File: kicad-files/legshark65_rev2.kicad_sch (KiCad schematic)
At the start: 199 parts, among them J1 ARM JTAG, SW1 K2-1187SQ-A4SW-06, SW2 PCM12SMTR, T2 53261-0471, U1 STM32F411CEU6, U2 MCP1700T-3302E/TT, U3 AT24C256C-SSHL-T, Y1 TAXM8M4RFDCET2T

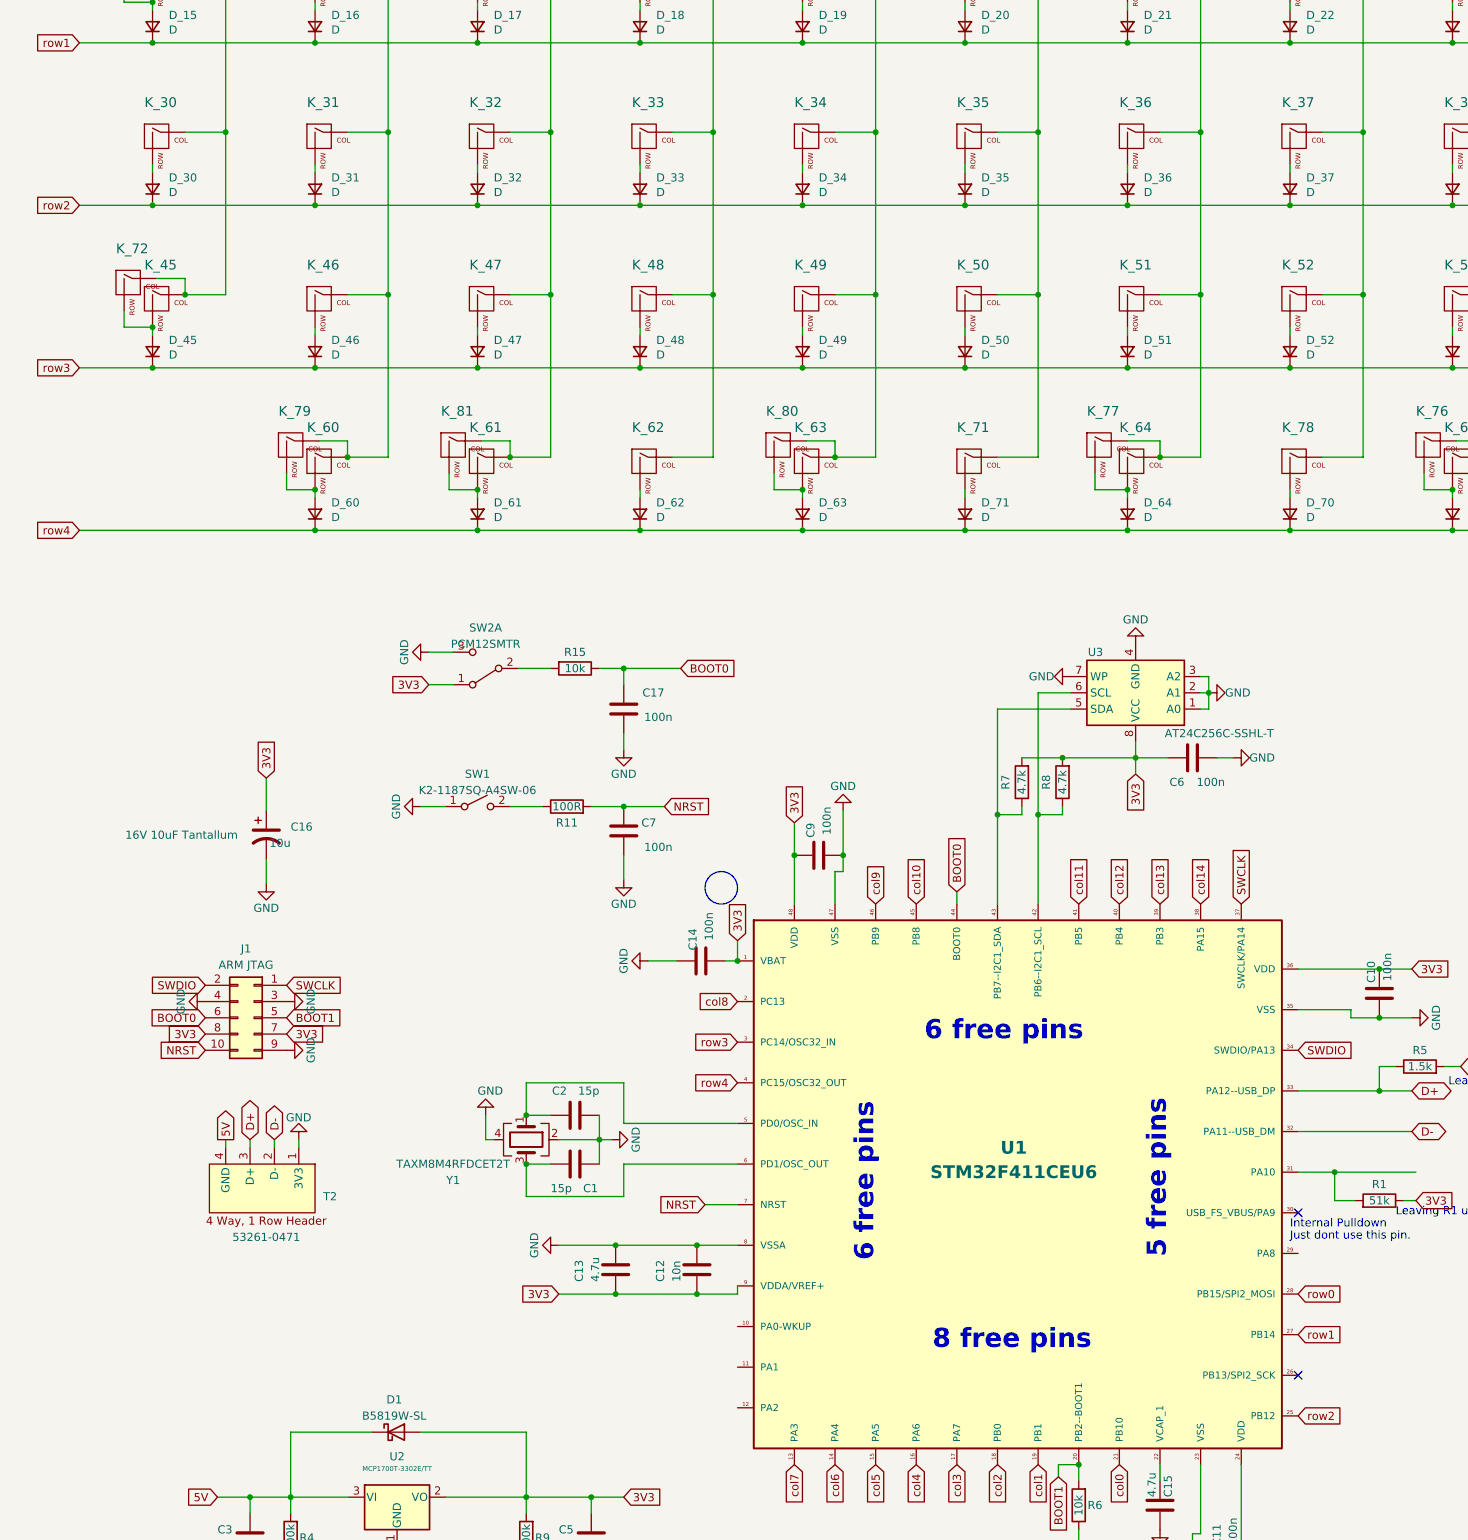
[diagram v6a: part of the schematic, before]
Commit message: Making the tracks have a more consistant width
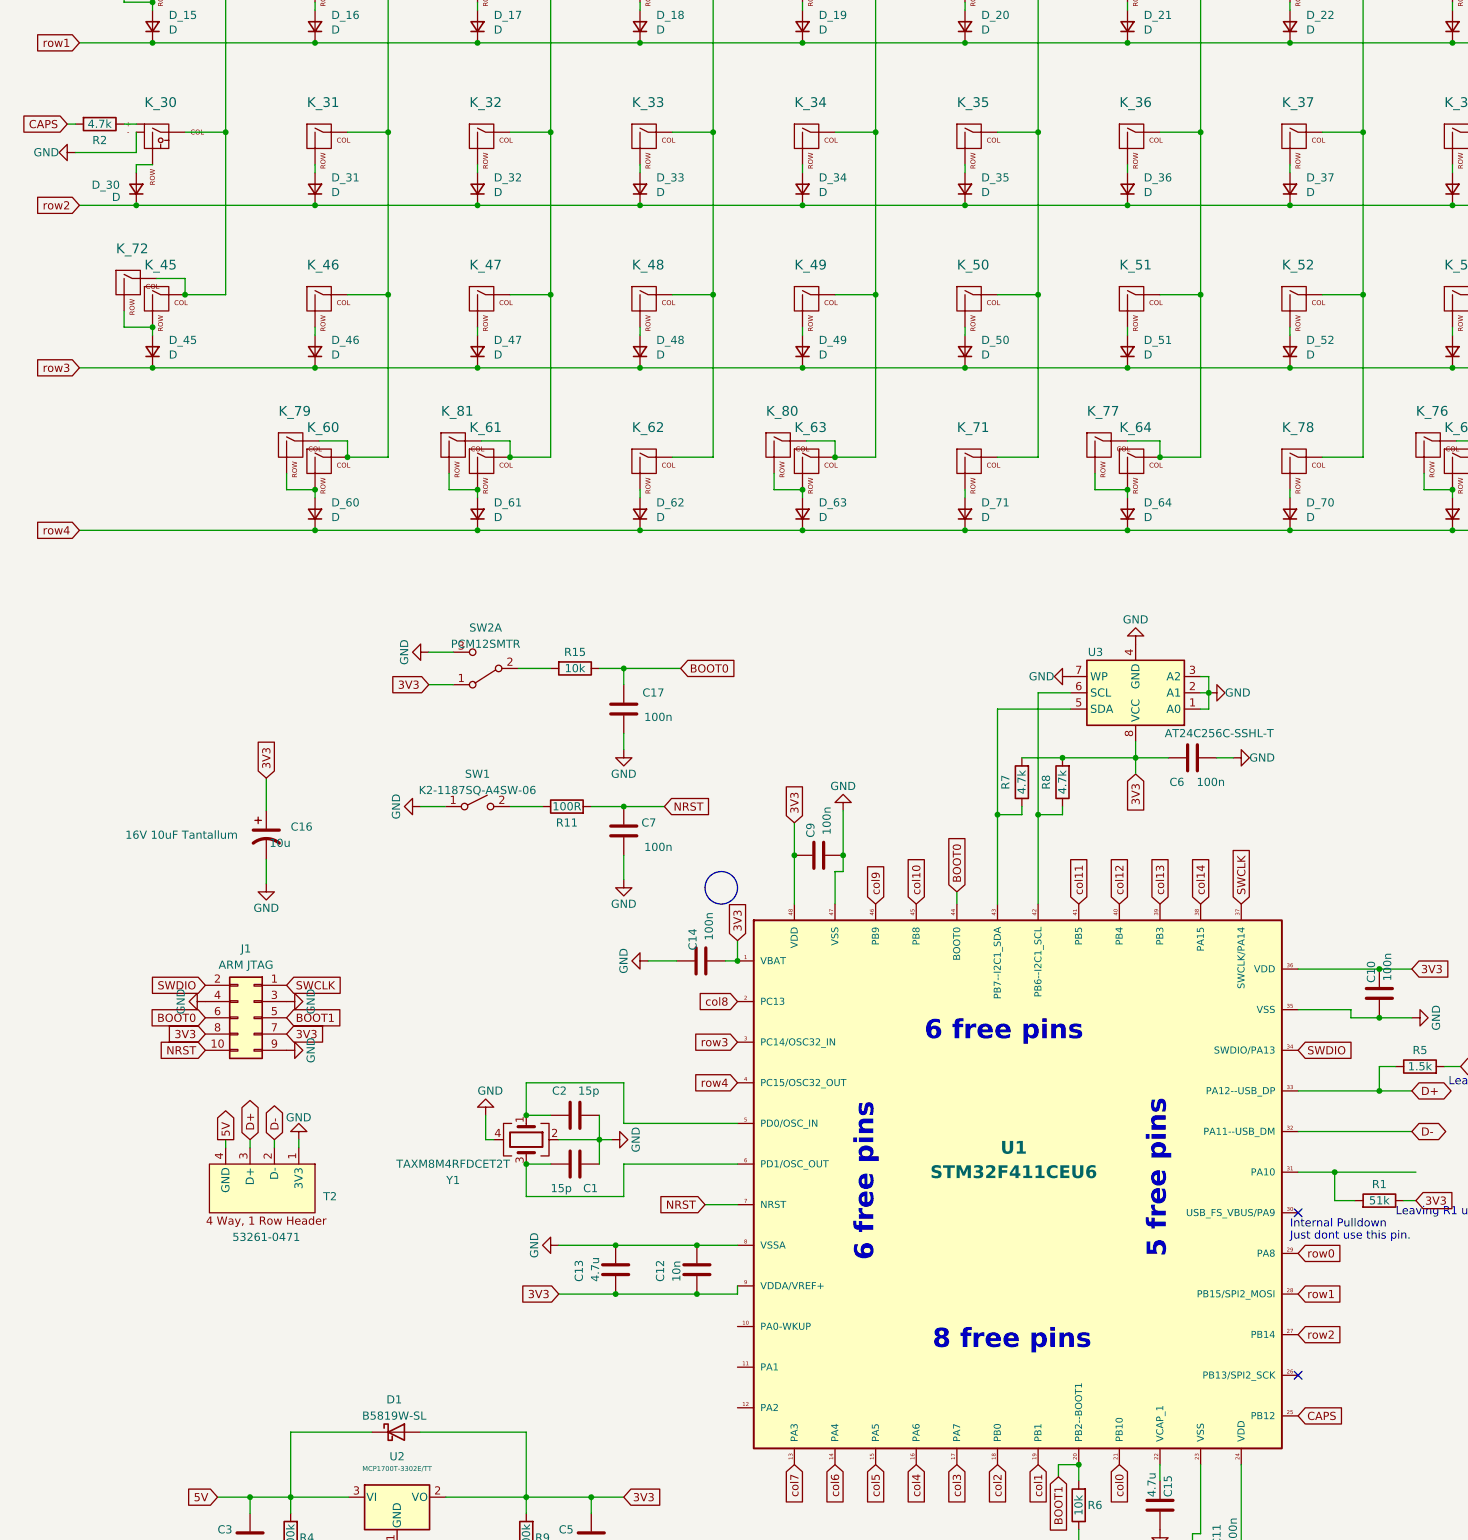
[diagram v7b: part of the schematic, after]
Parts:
- added R2: 4.7k, Resistor_SMD:R_0402_1005Metric_Pad0.72x0.64mm_HandSolder, symbol Device:R
- K_30: footprint MX_Only:MXOnly-1U-NoLED -> MX_Only:MXOnly-1U; symbol MX_Alps_Hybrid:MX-NoLED -> MX_Alps_Hybrid:MX-LED
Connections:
- net GND: now also K_30.4 (LEDGND)
- net row0: now also U1.29 (PA8); no longer U1.28 (PB15/SPI2_MOSI)
- net row1: now also U1.28 (PB15/SPI2_MOSI); no longer U1.27 (PB14)
- net row2: now also U1.27 (PB14); no longer U1.25 (PB12)
- new net: K_30.3 (LED), R2.1
- new net CAPS: R2.2, U1.25 (PB12)
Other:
- moved on the sheet: D_30
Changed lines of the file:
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@@
   (junction (at 237.49 60.96) (diameter 0) (color 0 0 0 0)
   )
-  (junction (at 34.29 86.36) (diameter 0) (color 0 0 0 0)
-  )
   (junction (at 186.69 86.36) (diameter 0) (color 0 0 0 0)
   )
@@
   (junction (at 223.52 74.93) (diameter 0) (color 0 0 0 0)
   )
+  (junction (at 31.75 86.36) (diameter 0) (color 0 0 0 0)
+  )
   (junction (at 364.49 35.56) (diameter 0) (color 0 0 0 0)
   )
@@
     (stroke (width 0) (type default))
   )
+  (wire (pts (xy 31.75 78.105) (xy 31.75 74.93))
+    (stroke (width 0) (type default))
+  )
   (wire (pts (xy 219.075 237.49) (xy 231.775 237.49))
     (stroke (width 0) (type default))
@@
     (stroke (width 0) (type default))
   )
+  (wire (pts (xy 29.845 73.66) (xy 31.75 73.66))
+    (stroke (width 0) (type default))
+  )
   (wire (pts (xy 288.29 35.56) (xy 313.69 35.56))
     (stroke (width 0) (type default))
@@
     (stroke (width 0) (type default))
   )
+  (wire (pts (xy 20.955 73.66) (xy 22.225 73.66))
+    (stroke (width 0) (type default))
+  )
   (wire (pts (xy 375.92 16.51) (xy 375.92 24.13))
     (stroke (width 0) (type default))
@@
     (stroke (width 0) (type default))
   )
-  (wire (pts (xy 34.29 86.36) (xy 59.69 86.36))
+  (wire (pts (xy 31.75 86.36) (xy 59.69 86.36))
     (stroke (width 0) (type default))
   )
@@
     (stroke (width 0) (type default))
   )
+  (wire (pts (xy 34.29 80.01) (xy 31.75 80.01))
+    (stroke (width 0) (type default))
+  )
   (wire (pts (xy 106.68 256.54) (xy 119.38 256.54))
     (stroke (width 0) (type default))
@@
     (stroke (width 0) (type default))
   )
+  (wire (pts (xy 31.75 80.01) (xy 31.75 81.28))
+    (stroke (width 0) (type default))
+  )
   (wire (pts (xy 172.72 100.33) (xy 172.72 74.93))
     (stroke (width 0) (type default))
@@
     (stroke (width 0) (type default))
   )
-  (wire (pts (xy 34.29 80.01) (xy 34.29 81.28))
-    (stroke (width 0) (type default))
-  )
   (wire (pts (xy 369.57 100.33) (xy 375.92 100.33))
     (stroke (width 0) (type default))
@@
     (stroke (width 0) (type default))
   )
+  (wire (pts (xy 22.225 78.105) (xy 31.75 78.105))
+    (stroke (width 0) (type default))
+  )
   (wire (pts (xy 161.29 60.96) (xy 186.69 60.96))
     (stroke (width 0) (type default))
@@
     (stroke (width 0) (type default))
   )
-  (wire (pts (xy 22.86 86.36) (xy 34.29 86.36))
+  (wire (pts (xy 22.86 86.36) (xy 31.75 86.36))
     (stroke (width 0) (type default))
   )
@@
     )
   )
+  (global_label "CAPS" (shape input) (at 213.36 275.59 0) (fields_autoplaced)
+    (effects (font (size 1.27 1.27)) (justify left))
+    (property "Intersheetrefs" "${INTERSHEET_REFS}" (at 220.4497 275.59 0)
+      (effects (font (size 1.27 1.27)) (justify left) hide)
+    )
+  )
   (global_label "3V3" (shape input) (at 204.47 301.625 270) (fields_autoplaced)
     (effects (font (size 1.27 1.27)) (justify right))
@@
     )
   )
-  (global_label "row0" (shape input) (at 213.36 256.54 0)
+  (global_label "row0" (shape input) (at 213.36 250.19 0)
     (effects (font (size 1.27 1.27)) (justify left))
-    (property "Intersheetrefs" "${INTERSHEET_REFS}" (at 213.36 256.54 0)
+    (property "Intersheetrefs" "${INTERSHEET_REFS}" (at 213.36 250.19 0)
       (effects (font (size 1.27 1.27)) hide)
     )
@@
     )
   )
-  (global_label "row1" (shape input) (at 213.36 262.89 0)
+  (global_label "row1" (shape input) (at 213.36 256.54 0)
     (effects (font (size 1.27 1.27)) (justify left))
-    (property "Intersheetrefs" "${INTERSHEET_REFS}" (at 213.36 262.89 0)
+    (property "Intersheetrefs" "${INTERSHEET_REFS}" (at 213.36 256.54 0)
       (effects (font (size 1.27 1.27)) hide)
     )
@@
     )
   )
+  (global_label "CAPS" (shape input) (at 20.955 73.66 180) (fields_autoplaced)
+    (effects (font (size 1.27 1.27)) (justify right))
+    (property "Intersheetrefs" "${INTERSHEET_REFS}" (at 13.8653 73.66 0)
+      (effects (font (size 1.27 1.27)) (justify right) hide)
+    )
+  )
   (global_label "3V3" (shape input) (at 187.96 175.26 270) (fields_autoplaced)
     (effects (font (size 1.27 1.27)) (justify right))
@@
     )
   )
-  (global_label "row2" (shape input) (at 213.36 275.59 0)
+  (global_label "row2" (shape input) (at 213.36 262.89 0)
     (effects (font (size 1.27 1.27)) (justify left))
-    (property "Intersheetrefs" "${INTERSHEET_REFS}" (at 213.36 275.59 0)
+    (property "Intersheetrefs" "${INTERSHEET_REFS}" (at 213.36 262.89 0)
       (effects (font (size 1.27 1.27)) hide)
     )
@@
     )
   )
-  (symbol (lib_id "Device:D_Small") (at 34.29 83.82 90) (unit 1)
+  (symbol (lib_id "power:GND") (at 22.225 78.105 270) (unit 1)
+    (in_bom yes) (on_board yes) (dnp no)
+    (property "Reference" "#PWR034" (at 15.875 78.105 0)
+      (effects (font (size 1.27 1.27)) hide)
+    )
+    (property "Value" "GND" (at 19.685 78.105 90)
+      (effects (font (size 1.27 1.27)) (justify right))
+    )
+    (property "Footprint" "" (at 22.225 78.105 0)
+      (effects (font (size 1.27 1.27)) hide)
+    )
+    (property "Datasheet" "" (at 22.225 78.105 0)
+      (effects (font (size 1.27 1.27)) hide)
+    )
+    (pin "1")
+    (instances
+      (project "legshark65_rev2"
+        (path "/2fcc1073-d3f4-43f9-b3b4-5cee13272705"
+          (reference "#PWR034") (unit 1)
+        )
+      )
+      (project "old_layout"
+        (path "/2fda2561-53ed-4930-8b41-858e0e3dd5f4"
+          (reference "#PWR019") (unit 1)
+        )
+      )
+      (project "legshark65_rev1"
+        (path "/9ddf6dc5-8b5e-413a-9b25-d1d5a5a60469"
+          (reference "#PWR020") (unit 1)
+        )
+      )
+    )
+  )
+  (symbol (lib_id "Device:D_Small") (at 31.75 83.82 90) (unit 1)
     (in_bom yes) (on_board yes) (dnp no)
-    (property "Reference" "D_30" (at 36.83 82.042 90)
+    (property "Reference" "D_30" (at 24.765 83.185 90)
       (effects (font (size 1.27 1.27)) (justify right))
     )
-    (property "Value" "D" (at 36.83 84.328 90)
+    (property "Value" "D" (at 27.94 85.09 90)
       (effects (font (size 1.27 1.27)) (justify right))
     )
-    (property "Footprint" "Diode_SMD:D_SOD-523" (at 35.56 91.44 0)
+    (property "Footprint" "Diode_SMD:D_SOD-523" (at 33.02 91.44 0)
       (effects (font (size 1.27 1.27)) hide)
     )
-    (property "Datasheet" "~" (at 35.56 91.44 0)
+    (property "Datasheet" "~" (at 33.02 91.44 0)
       (effects (font (size 1.27 1.27)) hide)
     )
@@
     )
   )
-  (symbol (lib_id "MX_Alps_Hybrid:MX-NoLED") (at 35.56 76.2 0) (unit 1)
+  (symbol (lib_id "MX_Alps_Hybrid:MX-LED") (at 35.56 76.2 0) (unit 1)
     (in_bom yes) (on_board yes) (dnp no)
     (property "Reference" "K_30" (at 35.56 70.2818 0)
       (effects (font (size 1.524 1.524)))
     )
-    (property "Value" "KEYSW" (at 35.56 78.74 0)
+    (property "Value" "KEYSW" (at 34.29 78.74 0)
       (effects (font (size 1.524 1.524)) hide)
     )
-    (property "Footprint" "MX_Only:MXOnly-1U-NoLED" (at 35.56 76.2 0)
+    (property "Footprint" "MX_Only:MXOnly-1U" (at 19.685 76.835 0)
       (effects (font (size 1.524 1.524)) hide)
     )
-    (property "Datasheet" "" (at 35.56 76.2 0)
-      (effects (font (size 1.524 1.524)))
+    (property "Datasheet" "" (at 19.685 76.835 0)
+      (effects (font (size 1.524 1.524)) hide)
     )
     (pin "1")
     (pin "2")
+    (pin "3")
+    (pin "4")
     (instances
       (project "legshark65_rev2"
@@
         )
       )
+    )
+  )
+  (symbol (lib_id "Device:R") (at 26.035 73.66 270) (unit 1)
+    (in_bom yes) (on_board yes) (dnp no)
+    (property "Reference" "R2" (at 26.035 76.2 90)
+      (effects (font (size 1.27 1.27)))
+    )
+    (property "Value" "4.7k" (at 26.035 73.66 90)
+      (effects (font (size 1.27 1.27)))
+    )
+    (property "Footprint" "Resistor_SMD:R_0402_1005Metric_Pad0.72x0.64mm_HandSolder" (at 26.035 71.882 90)
+      (effects (font (size 1.27 1.27)) hide)
+    )
+    (property "Datasheet" "~" (at 26.035 73.66 0)
+      (effects (font (size 1.27 1.27)) hide)
+    )
+    (property "LCSC Part" "C23162" (at 26.035 73.66 0)
+      (effects (font (size 1.27 1.27)) hide)
+    )
+    (property "Manufacturer" "Uniroyal Elec" (at 26.035 73.66 0)
+      (effects (font (size 1.27 1.27)) hide)
+    )
+    (property "Manufacturer Part Number" "0603WAF4701T5E" (at 26.035 73.66 0)
+      (effects (font (size 1.27 1.27)) hide)
+    )
+    (property "Package" "0603" (at 26.035 73.66 0)
+      (effects (font (size 1.27 1.27)) hide)
+    )
+    (property "Specification" "±1% 4.7kΩ 0603 Chip Resistor" (at 26.035 73.66 0)
+      (effects (font (size 1.27 1.27)) hide)
+    )
+    (property "Vendor Part Number" "LCSC C23162" (at 26.035 73.66 0)
+      (effects (font (size 1.27 1.27)) hide)
+    )
+    (pin "1")
+    (pin "2")
+    (instances
+      (project "legshark65_rev2"
+        (path "/2fcc1073-d3f4-43f9-b3b4-5cee13272705"
+          (reference "R2") (unit 1)
+        )
+      )
+      (project "old_layout"
+        (path "/2fda2561-53ed-4930-8b41-858e0e3dd5f4"
+          (reference "R7") (unit 1)
+        )
+      )
+      (project "legshark65_rev1"
+        (path "/9ddf6dc5-8b5e-413a-9b25-d1d5a5a60469"
+          (reference "R7") (unit 1)
+        )
+      )

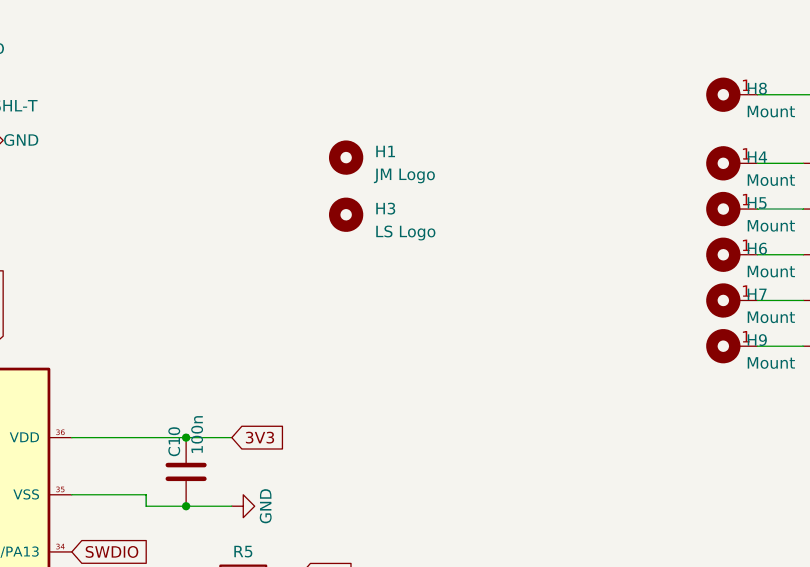
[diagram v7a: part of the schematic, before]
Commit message: Added outline legshark logo
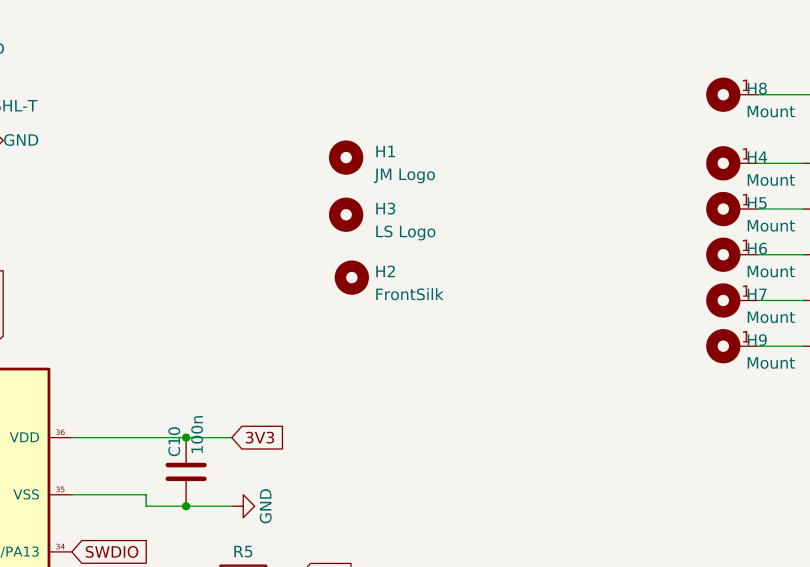
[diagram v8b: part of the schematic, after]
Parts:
- added H2: FrontSilk, Legshark:Legshark_Logo_Huge, symbol Mechanical:MountingHole
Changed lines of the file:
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@@
+    )
+  )
+  (symbol (lib_id "Mechanical:MountingHole") (at 244.475 187.96 0) (unit 1)
+    (in_bom yes) (on_board yes) (dnp no) (fields_autoplaced)
+    (property "Reference" "H2" (at 247.015 187.325 0)
+      (effects (font (size 1.27 1.27)) (justify left))
+    )
+    (property "Value" "FrontSilk" (at 247.015 189.865 0)
+      (effects (font (size 1.27 1.27)) (justify left))
+    )
+    (property "Footprint" "Legshark:Legshark_Logo_Huge" (at 244.475 187.96 0)
+      (effects (font (size 1.27 1.27)) hide)
+    )
+    (property "Datasheet" "~" (at 244.475 187.96 0)
+      (effects (font (size 1.27 1.27)) hide)
+    )
+    (instances
+      (project "legshark65_rev2"
+        (path "/2fcc1073-d3f4-43f9-b3b4-5cee13272705"
+          (reference "H2") (unit 1)
+        )
+      )
+      (project "legshark65_rev1"
+        (path "/9ddf6dc5-8b5e-413a-9b25-d1d5a5a60469"
+          (reference "H3") (unit 1)
+        )
+      )
     )
   )
